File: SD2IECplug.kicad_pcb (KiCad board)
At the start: 2 copper layers, 50 x 49.4 mm, 49 parts, among them J1 ISP, J2 X6, J3 Aux, J4 IEC, J5 C64-CassettePort, J6 C64-CassettePort, J7 Power, J8 X3, Q1 IRLML2803, Q2 IRLML2803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

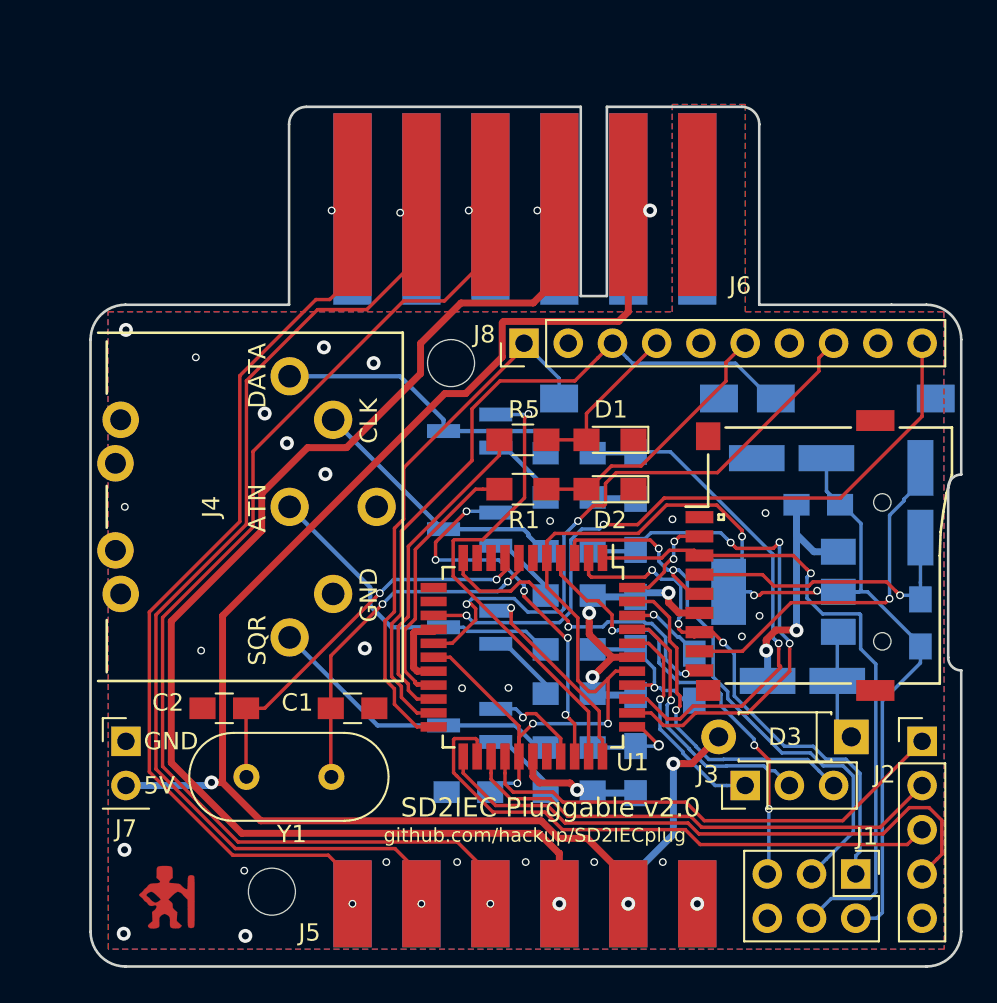
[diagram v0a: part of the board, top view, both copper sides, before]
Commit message: Corrected ground plane.
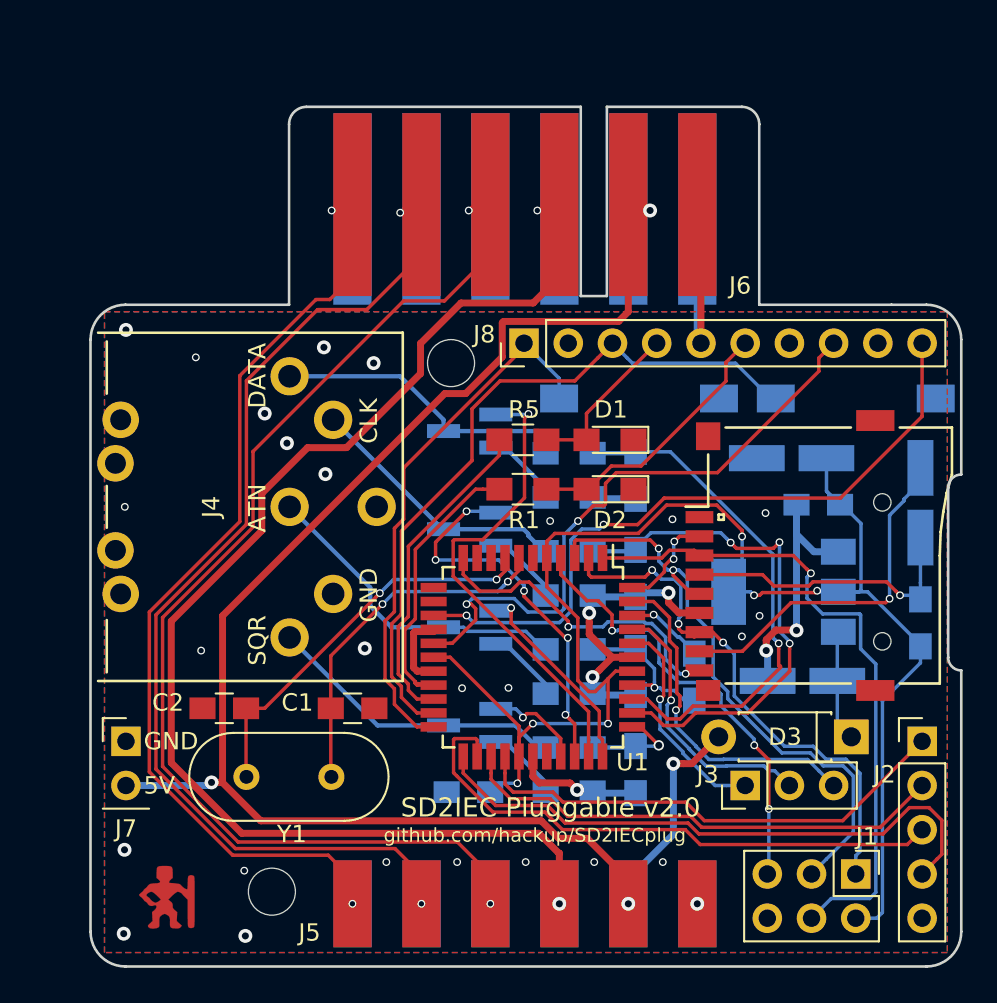
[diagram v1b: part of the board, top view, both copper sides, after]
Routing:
- net Cas-GND: track 49.0 -> 64.8 mm
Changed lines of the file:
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@@
     (thickness 1.6)
     (drawings 36)
-    (tracks 810)
+    (tracks 814)
     (zones 0)
     (modules 49)
@@
     (mod_text_size 1 1)
     (mod_text_width 0.15)
-    (pad_size 2.7 1.1)
-    (pad_drill 2.7)
+    (pad_size 2.2 10.5)
+    (pad_drill 0)
     (pad_to_mask_clearance 0.2)
     (aux_axis_origin 94 53.354)
@@
     (add_net Cas-Motor)
   )
+  (module hackup:C64-Cassette-Port-Male (layer F.Cu)
+    (at 116.4 53.354)
+    (fp_text reference J6 (at 12.9 -1.1) (layer F.SilkS)
+      (effects (font (size 1 1) (thickness 0.15)))
+    )
+    (fp_text value C64-CassettePort (at 1 1) (layer F.Fab)
+      (effects (font (size 1 1) (thickness 0.15)))
+    )
+    (fp_poly (pts (xy -13.1 -12.1) (xy 14.1 -12.1) (xy 14.1 -0.7) (xy -13.1 -0.7)) (layer F.Mask) (width 0.15))
+    (fp_poly (pts (xy -13.1 -12.1) (xy 14.1 -12.1) (xy 14.1 -0.6) (xy -13.1 -0.6)) (layer B.Mask) (width 0.15))
+    (fp_line (start 14 0) (end 14 -11.5) (layer F.CrtYd) (width 0.15))
+    (fp_line (start 3.75 -12) (end -12.5 -12) (layer F.CrtYd) (width 0.15))
+    (fp_line (start 3.75 -0.25) (end 3.75 -12) (layer F.CrtYd) (width 0.15))
+    (fp_line (start 5.25 -0.25) (end 3.75 -0.25) (layer F.CrtYd) (width 0.15))
+    (fp_line (start 5.25 -12) (end 5.25 -0.25) (layer F.CrtYd) (width 0.15))
+    (fp_line (start 13.5 -12) (end 5.25 -12) (layer F.CrtYd) (width 0.15))
+    (fp_line (start -13 0) (end 14 0) (layer F.CrtYd) (width 0.15))
+    (fp_line (start -13 -11.5) (end -13 0) (layer F.CrtYd) (width 0.15))
+    (fp_arc (start 13.5 -11.5) (end 13.5 -12) (angle 90) (layer F.CrtYd) (width 0.15))
+    (fp_arc (start -12.5 -11.5) (end -13 -11.5) (angle 90) (layer F.CrtYd) (width 0.15))
+    (pad F smd rect (at -9.36 -5.5) (size 2.2 11) (layers B.Cu B.Mask)
+      (net 30 Cas-Sense))
+    (pad E smd rect (at -5.4 -5.5) (size 2.2 11) (layers B.Cu B.Mask)
+      (net 29 Cas-Write))
+    (pad D smd rect (at -1.44 -5.5) (size 2.2 11) (layers B.Cu B.Mask)
+      (net 28 Cas-Read))
+    (pad C smd rect (at 2.52 -5.5) (size 2.2 11) (layers B.Cu B.Mask)
+      (net 27 Cas-Motor))
+    (pad B smd rect (at 6.48 -5.5) (size 2.2 11) (layers B.Cu B.Mask)
+      (net 26 Cas-5V))
+    (pad A smd rect (at 10.44 -5.5) (size 2.2 11) (layers B.Cu B.Mask)
+      (net 25 Cas-GND))
+    (pad 6 smd rect (at -9.36 -5.75) (size 2.2 10.5) (layers F.Cu F.Mask)
+      (net 30 Cas-Sense))
+    (pad 5 smd rect (at -5.4 -5.75) (size 2.2 10.5) (layers F.Cu F.Mask)
+      (net 29 Cas-Write))
+    (pad 4 smd rect (at -1.44 -5.75) (size 2.2 10.5) (layers F.Cu F.Mask)
+      (net 28 Cas-Read))
+    (pad 3 smd rect (at 2.52 -5.75) (size 2.2 10.5) (layers F.Cu F.Mask)
+      (net 27 Cas-Motor))
+    (pad 2 smd rect (at 6.48 -5.75) (size 2.2 10.5) (layers F.Cu F.Mask)
+      (net 26 Cas-5V))
+    (pad 1 smd rect (at 10.44 -5.75) (size 2.2 10.5) (layers F.Cu F.Mask)
+      (net 25 Cas-GND))
+  )
   (module DIN-Connectors:DIN-6-Variable (layer F.Cu)
     (at 103.43 64.96 90)
@@
     (pad "" np_thru_hole oval (at 0 0) (size 2.7 1.1) (drill oval 2.7 1.1) (layers *.Cu *.Mask))
   )
-  (module hackup:C64-Cassette-Port-Male (layer F.Cu)
-    (at 116.4 53.354)
-    (fp_text reference J6 (at 12.9 -1.1) (layer F.SilkS)
-      (effects (font (size 1 1) (thickness 0.15)))
-    )
-    (fp_text value C64-CassettePort (at 1 1) (layer F.Fab)
-      (effects (font (size 1 1) (thickness 0.15)))
-    )
-    (fp_arc (start -12.5 -11.5) (end -13 -11.5) (angle 90) (layer F.CrtYd) (width 0.15))
-    (fp_arc (start 13.5 -11.5) (end 13.5 -12) (angle 90) (layer F.CrtYd) (width 0.15))
-    (fp_line (start -13 -11.5) (end -13 0) (layer F.CrtYd) (width 0.15))
-    (fp_line (start -13 0) (end 14 0) (layer F.CrtYd) (width 0.15))
-    (fp_line (start 13.5 -12) (end 5.25 -12) (layer F.CrtYd) (width 0.15))
-    (fp_line (start 5.25 -12) (end 5.25 -0.25) (layer F.CrtYd) (width 0.15))
-    (fp_line (start 5.25 -0.25) (end 3.75 -0.25) (layer F.CrtYd) (width 0.15))
-    (fp_line (start 3.75 -0.25) (end 3.75 -12) (layer F.CrtYd) (width 0.15))
-    (fp_line (start 3.75 -12) (end -12.5 -12) (layer F.CrtYd) (width 0.15))
-    (fp_line (start 14 0) (end 14 -11.5) (layer F.CrtYd) (width 0.15))
-    (pad 1 smd rect (at 10.44 -5.75) (size 2.2 10.5) (layers F.Cu F.Paste F.Mask)
-      (net 25 Cas-GND))
-    (pad 2 smd rect (at 6.48 -5.75) (size 2.2 10.5) (layers F.Cu F.Paste F.Mask)
-      (net 26 Cas-5V))
-    (pad 3 smd rect (at 2.52 -5.75) (size 2.2 10.5) (layers F.Cu F.Paste F.Mask)
-      (net 27 Cas-Motor))
-    (pad 4 smd rect (at -1.44 -5.75) (size 2.2 10.5) (layers F.Cu F.Paste F.Mask)
-      (net 28 Cas-Read))
-    (pad 5 smd rect (at -5.4 -5.75) (size 2.2 10.5) (layers F.Cu F.Paste F.Mask)
-      (net 29 Cas-Write))
-    (pad 6 smd rect (at -9.36 -5.75) (size 2.2 10.5) (layers F.Cu F.Paste F.Mask)
-      (net 30 Cas-Sense))
-    (pad A smd rect (at 10.44 -5.5) (size 2.2 11) (layers B.Cu B.Paste B.Mask)
-      (net 25 Cas-GND))
-    (pad B smd rect (at 6.48 -5.5) (size 2.2 11) (layers B.Cu B.Paste B.Mask)
-      (net 26 Cas-5V))
-    (pad C smd rect (at 2.52 -5.5) (size 2.2 11) (layers B.Cu B.Paste B.Mask)
-      (net 27 Cas-Motor))
-    (pad D smd rect (at -1.44 -5.5) (size 2.2 11) (layers B.Cu B.Paste B.Mask)
-      (net 28 Cas-Read))
-    (pad E smd rect (at -5.4 -5.5) (size 2.2 11) (layers B.Cu B.Paste B.Mask)
-      (net 29 Cas-Write))
-    (pad F smd rect (at -9.36 -5.5) (size 2.2 11) (layers B.Cu B.Paste B.Mask)
-      (net 30 Cas-Sense))
-  )
   (module Pin_Headers:Pin_Header_Straight_1x03_Pitch2.54mm (layer F.Cu)
     (at 129.592 80.962 90)
@@
   (segment (start 117.4 79.296) (end 117.4 80.446) (width 0.4) (layer F.Cu) (net 25))
   (segment (start 119.540001 80.816001) (end 119.94 81.216) (width 0.4) (layer F.Cu) (net 25))
+  (segment (start 127.052 47.816) (end 126.84 47.604) (width 0.4) (layer F.Cu) (net 25))
+  (segment (start 127.052 55.562) (end 127.052 47.816) (width 0.4) (layer F.Cu) (net 25))
+  (segment (start 126.84 55.35) (end 127.052 55.562) (width 0.4) (layer B.Cu) (net 25))
+  (segment (start 126.84 47.854) (end 126.84 55.35) (width 0.4) (layer B.Cu) (net 25))
   (via (at 124.131 47.942) (size 0.8) (drill 0.4) (layers F.Cu B.Cu) (net 26))
   (segment (start 122.88 47.854) (end 124.043 47.854) (width 0.4) (layer B.Cu) (net 26))
@@
     (polygon
       (pts
-        (xy 129.6 53.754) (xy 141 53.754) (xy 141.022 90.36) (xy 93.022 90.36) (xy 93 53.754)
-        (xy 125.4 53.754) (xy 125.4 41.854) (xy 129.6 41.854)
+        (xy 92.8 53.754) (xy 141.2 53.754) (xy 141.2 90.554) (xy 92.8 90.554)
       )
     )
@@
     (polygon
       (pts
-        (xy 129.6 53.754) (xy 141 53.754) (xy 141.022 90.36) (xy 93.022 90.36) (xy 93 53.754)
-        (xy 125.4 53.754) (xy 125.4 41.854) (xy 129.6 41.854)
+        (xy 92.8 53.754) (xy 141.2 53.754) (xy 141.2 90.554) (xy 92.8 90.554)
       )
     )
